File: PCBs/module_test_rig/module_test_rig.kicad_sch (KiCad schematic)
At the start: 16 parts, among them J101 STDC14, J102 10-Pin Pogo Connector, J103 TYPE-C-31-M-12, SW101 SW_SPDT, SW102 PSH_BTN, U101 Watch_Module_Outline_V1_SS, U102 AMS1117-3.3

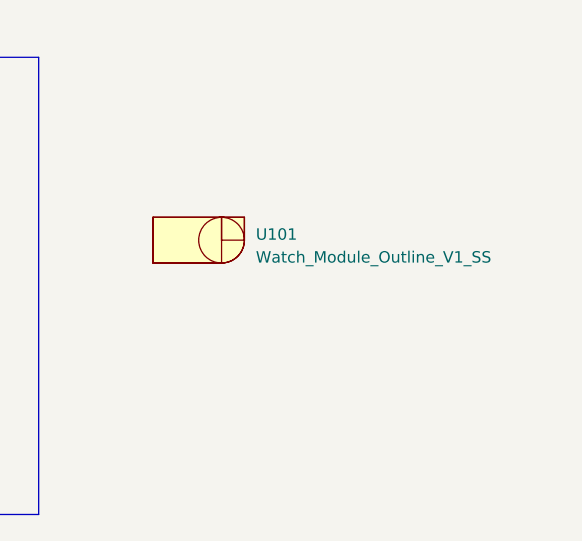
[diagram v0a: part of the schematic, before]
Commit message: RFID Module v1.1 complete (+default firmware)
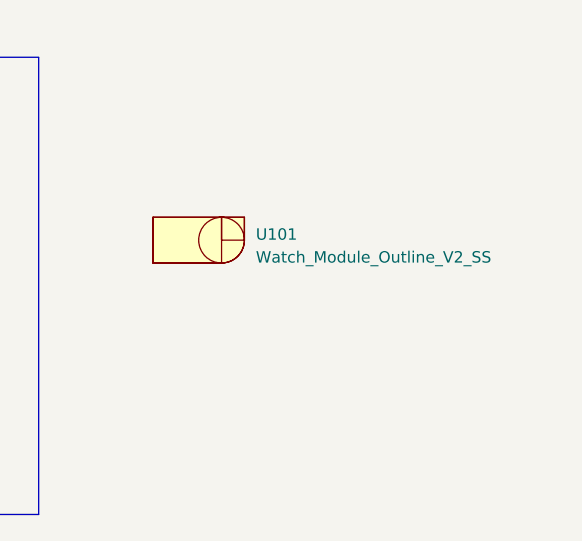
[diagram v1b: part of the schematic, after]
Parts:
- U101: value Watch_Module_Outline_V1_SS -> Watch_Module_Outline_V2_SS; footprint watch_footprints:Watch Module Outline V1 SS -> watch_footprints:Watch Module Outline V2 SS; symbol watch_symbols_lib:Watch_Module_Outline_V1_SS -> watch_symbols_lib:Watch_Module_Outline_V2_SS
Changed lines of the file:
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@@
     )
   )
-  (symbol (lib_id "watch_symbols_lib:Watch_Module_Outline_V1_SS") (at 223.52 48.26 0) (unit 1)
+  (symbol (lib_id "watch_symbols_lib:Watch_Module_Outline_V2_SS") (at 223.52 48.26 0) (unit 1)
     (in_bom no) (on_board yes) (dnp no) (fields_autoplaced)
     (property "Reference" "U101" (at 229.87 47.625 0)
       (effects (font (size 1.27 1.27)) (justify left))
     )
-    (property "Value" "Watch_Module_Outline_V1_SS" (at 229.87 50.165 0)
+    (property "Value" "Watch_Module_Outline_V2_SS" (at 229.87 50.165 0)
       (effects (font (size 1.27 1.27)) (justify left))
     )
-    (property "Footprint" "watch_footprints:Watch Module Outline V1 SS" (at 223.52 53.34 0)
+    (property "Footprint" "watch_footprints:Watch Module Outline V2 SS" (at 223.52 53.34 0)
       (effects (font (size 1.27 1.27)) hide)
     )
